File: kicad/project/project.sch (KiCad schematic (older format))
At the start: 42 parts, among them J1 SWD, J3 Voltmeter, U1 ADS1015, U2 AP7380, U3 STM32L031F4Px, U4 VN7003ALH

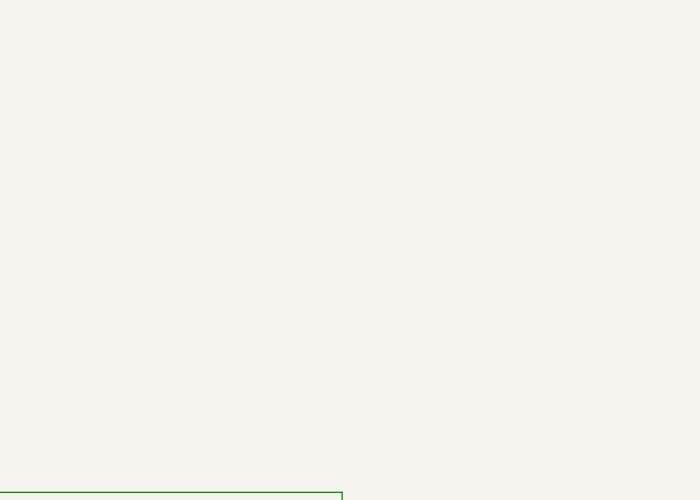
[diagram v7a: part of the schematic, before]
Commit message: Mounting holes
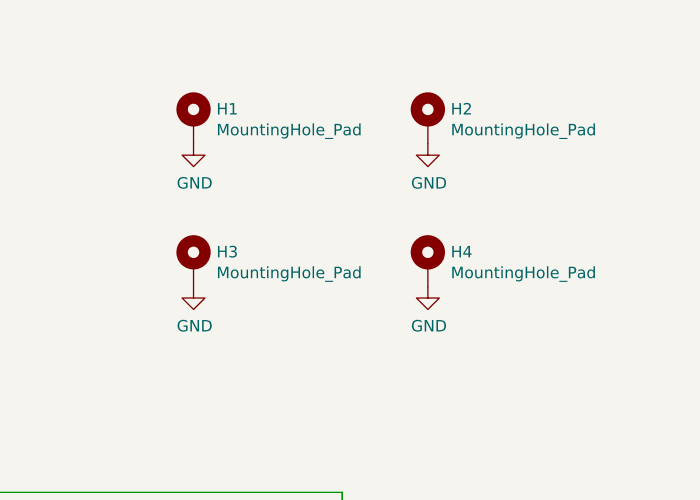
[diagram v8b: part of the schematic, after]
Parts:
- added H1, H2, H3, H4: MountingHole_Pad, MountingHole:MountingHole_3.2mm_M3_Pad, symbol Mechanical:MountingHole_Pad
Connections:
- net GND: now also H1.1, H2.1, H3.1, H4.1
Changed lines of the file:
@@
+	1    0    0    -1
+$EndComp
+$Comp
+L Mechanical:MountingHole_Pad H1
+U 1 1 5C8B15A7
+P 9000 1050
+F 0 "H1" H 9100 1101 50  0000 L CNN
+F 1 "MountingHole_Pad" H 9100 1010 50  0000 L CNN
+F 2 "MountingHole:MountingHole_3.2mm_M3_Pad" H 9000 1050 50  0001 C CNN
+F 3 "~" H 9000 1050 50  0001 C CNN
+	1    9000 1050
+	1    0    0    -1
+$EndComp
+$Comp
+L Mechanical:MountingHole_Pad H2
+U 1 1 5C8B1717
+P 10025 1050
+F 0 "H2" H 10125 1101 50  0000 L CNN
+F 1 "MountingHole_Pad" H 10125 1010 50  0000 L CNN
+F 2 "MountingHole:MountingHole_3.2mm_M3_Pad" H 10025 1050 50  0001 C CNN
+F 3 "~" H 10025 1050 50  0001 C CNN
+	1    10025 1050
+	1    0    0    -1
+$EndComp
+$Comp
+L Mechanical:MountingHole_Pad H3
+U 1 1 5C8B74C5
+P 9000 1675
+F 0 "H3" H 9100 1726 50  0000 L CNN
+F 1 "MountingHole_Pad" H 9100 1635 50  0000 L CNN
+F 2 "MountingHole:MountingHole_3.2mm_M3_Pad" H 9000 1675 50  0001 C CNN
+F 3 "~" H 9000 1675 50  0001 C CNN
+	1    9000 1675
+	1    0    0    -1
+$EndComp
+$Comp
+L Mechanical:MountingHole_Pad H4
+U 1 1 5C8B74CC
+P 10025 1675
+F 0 "H4" H 10125 1726 50  0000 L CNN
+F 1 "MountingHole_Pad" H 10125 1635 50  0000 L CNN
+F 2 "MountingHole:MountingHole_3.2mm_M3_Pad" H 10025 1675 50  0001 C CNN
+F 3 "~" H 10025 1675 50  0001 C CNN
+	1    10025 1675
+	1    0    0    -1
+$EndComp
+$Comp
+L power:GND #PWR034
+U 1 1 5C8BA2A9
+P 9000 1150
+F 0 "#PWR034" H 9000 900 50  0001 C CNN
+F 1 "GND" H 9005 977 50  0000 C CNN
+F 2 "" H 9000 1150 50  0001 C CNN
+F 3 "" H 9000 1150 50  0001 C CNN
+	1    9000 1150
+	1    0    0    -1
+$EndComp
+$Comp
+L power:GND #PWR037
+U 1 1 5C8BA36C
+P 10025 1150
+F 0 "#PWR037" H 10025 900 50  0001 C CNN
+F 1 "GND" H 10030 977 50  0000 C CNN
+F 2 "" H 10025 1150 50  0001 C CNN
+F 3 "" H 10025 1150 50  0001 C CNN
+	1    10025 1150
+	1    0    0    -1
+$EndComp
+$Comp
+L power:GND #PWR039
+U 1 1 5C8BA3D3
+P 10025 1775
+F 0 "#PWR039" H 10025 1525 50  0001 C CNN
+F 1 "GND" H 10030 1602 50  0000 C CNN
+F 2 "" H 10025 1775 50  0001 C CNN
+F 3 "" H 10025 1775 50  0001 C CNN
+	1    10025 1775
+	1    0    0    -1
+$EndComp
+$Comp
+L power:GND #PWR038
+U 1 1 5C8BA43A
+P 9000 1775
+F 0 "#PWR038" H 9000 1525 50  0001 C CNN
+F 1 "GND" H 9005 1602 50  0000 C CNN
+F 2 "" H 9000 1775 50  0001 C CNN
+F 3 "" H 9000 1775 50  0001 C CNN
+	1    9000 1775
 	1    0    0    -1
 $EndComp
